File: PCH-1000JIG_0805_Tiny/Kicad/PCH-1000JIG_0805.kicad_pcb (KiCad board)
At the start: 2 copper layers, 23.1 x 11.3 mm, 14 parts

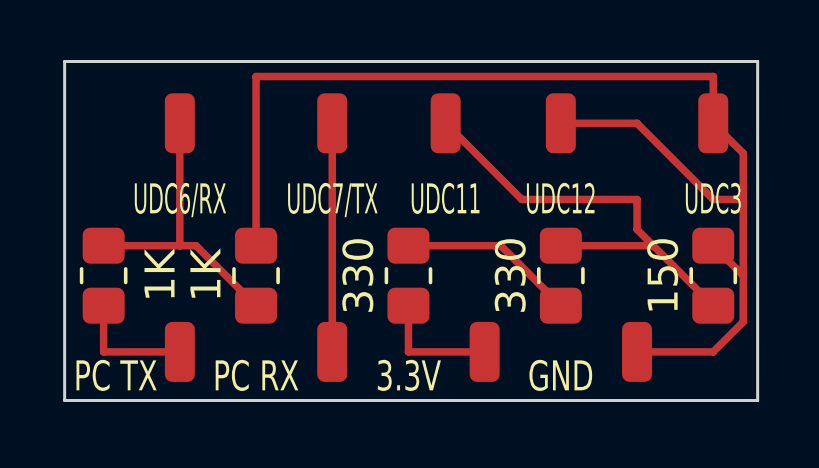
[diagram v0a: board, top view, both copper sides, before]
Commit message: Revision 2.2a of the tiny board.
Footprint reduced from 23.1 x 11.3mm(0.91 x 0.44 inches) to 19.3 x 11mm(0.76 x 0.43 inches)
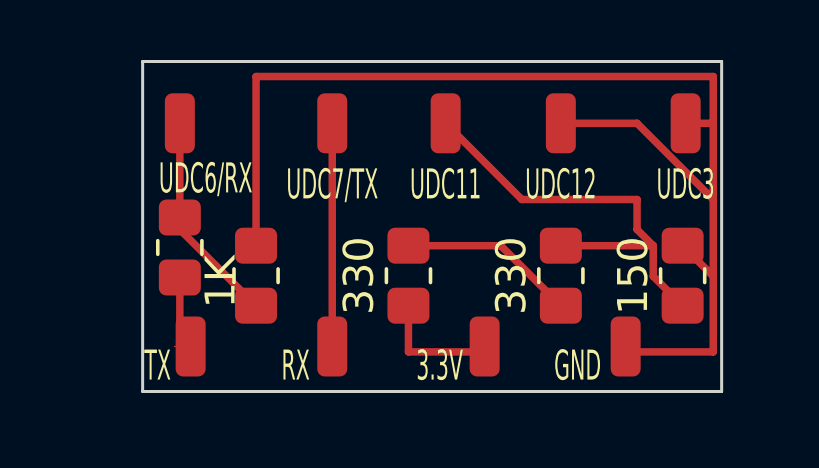
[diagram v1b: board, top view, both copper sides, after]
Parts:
- RX: renamed from PC RX
- TX: renamed from PC TX
- moved 1K 2.71 mm to (40.6, 39.7)
- moved 150 1.02 mm to (57.4, 40.6)
- moved UDC3 0.92 mm to (57.5, 35.6)
- moved GND 0.42 mm to (55.5, 43.0)
- moved TX 0.40 mm to (41.0, 43.0)
- moved 3.3V 0.18 mm to (50.8, 43.0)
- moved RX 0.18 mm to (45.7, 43.0)
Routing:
- net (no net): track 88.8 -> 84.7 mm
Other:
- board size 23.1 x 11.3 mm -> 19.3 x 11 mm
- board text added: "PCH-1000JIG Rev 2.2a by Mathieulh"
- board text removed: "PCH-1000JIG Rev 2.1a by Mathieulh"

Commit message: Changed silkscreen
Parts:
- PC RX: renamed from RX
- PC TX: renamed from TX
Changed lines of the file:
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@@
     (tags "MesurementPoint Square SMDPad 1mmx2mm ")
     (attr exclude_from_pos_files exclude_from_bom)
-    (fp_text reference "3.3V" (at -1.5 0.64) (layer "F.SilkS")
+    (fp_text reference "3.3V" (at 1.6 0.64) (layer "F.SilkS")
         (effects (font (size 1 0.5) (thickness 0.15)))
     )
@@
     (tags "MesurementPoint Square SMDPad 1mmx2mm ")
     (attr exclude_from_pos_files exclude_from_bom)
-    (fp_text reference "RX" (at -1.22 0.64) (layer "F.SilkS")
+    (fp_text reference "PC RX" (at 1.88 0.64) (layer "F.SilkS")
         (effects (font (size 1 0.5) (thickness 0.15)))
     )
@@
     (tags "MesurementPoint Square SMDPad 1mmx2mm ")
     (attr exclude_from_pos_files exclude_from_bom)
-    (fp_text reference "GND" (at -1.6 0.64) (layer "F.SilkS")
+    (fp_text reference "GND" (at 1.6 0.64) (layer "F.SilkS")
         (effects (font (size 1 0.5) (thickness 0.15)))
     )
@@
     (tags "MesurementPoint Square SMDPad 1mmx2mm ")
     (attr exclude_from_pos_files exclude_from_bom)
-    (fp_text reference "TX" (at -1.1 0.64) (layer "F.SilkS")
+    (fp_text reference "PC TX" (at 1.9 0.64) (layer "F.SilkS")
         (effects (font (size 1 0.5) (thickness 0.15)))
     )

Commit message: fixed a trace
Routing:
- net (no net): track 84.7 -> 88.7 mm
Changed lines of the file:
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@@
   (segment (start 52.04 38.1) (end 49.5 35.56) (width 0.25) (layer "F.Cu") (net 0))
   (segment (start 55.88 39.1) (end 55.88 38.1) (width 0.25) (layer "F.Cu") (net 0))
+  (segment (start 40.64 39.1) (end 42.68 41.14) (width 0.25) (layer "F.Cu") (net 0))
+  (segment (start 41.8 35.56) (end 41.8 40.26) (width 0.25) (layer "F.Cu") (net 0))
   (segment (start 48.26 39.64) (end 51.34 39.64) (width 0.25) (layer "F.Cu") (net 0))
   (segment (start 40.64 40.7) (end 40.64 42.64) (width 0.25) (layer "F.Cu") (net 0))
@@
   (segment (start 41 43) (end 40.46 43) (width 0) (layer "F.Cu") (net 0))
   (segment (start 40.64 42.64) (end 41 43) (width 0) (layer "F.Cu") (net 0))
-  (segment (start 40.64 39.1) (end 43.18 41.64) (width 0.25) (layer "F.Cu") (net 0))
-  (segment (start 40.64 35.56) (end 40.64 38.7) (width 0.25) (layer "F.Cu") (net 0))
   (segment (start 41 40.86) (end 40.64 40.5) (width 0) (layer "F.Cu") (net 0))
   (segment (start 56.42 39.64) (end 55.88 39.1) (width 0.25) (layer "F.Cu") (net 0))
   (segment (start 55.88 38.1) (end 52.04 38.1) (width 0.25) (layer "F.Cu") (net 0))
   (segment (start 48.26 41.64) (end 48.26 43.18) (width 0.25) (layer "F.Cu") (net 0))
+  (segment (start 40.64 35.56) (end 41.8 35.56) (width 0.25) (layer "F.Cu") (net 0))
   (segment (start 58.4 40.64) (end 57.4 39.64) (width 0.25) (layer "F.Cu") (net 0))
+  (segment (start 41.8 40.26) (end 42.68 41.14) (width 0.25) (layer "F.Cu") (net 0))
   (segment (start 58.42 35.56) (end 58.42 38.1) (width 0.25) (layer "F.Cu") (net 0))
   (segment (start 53.34 35.56) (end 55.88 35.56) (width 0.25) (layer "F.Cu") (net 0))
   (segment (start 50.62 43.18) (end 50.8 43) (width 0.25) (layer "F.Cu") (net 0))
+  (segment (start 42.68 41.14) (end 43.18 41.64) (width 0.25) (layer "F.Cu") (net 0))
   (segment (start 45.72 35.56) (end 45.72 43) (width 0.25) (layer "F.Cu") (net 0))
 )

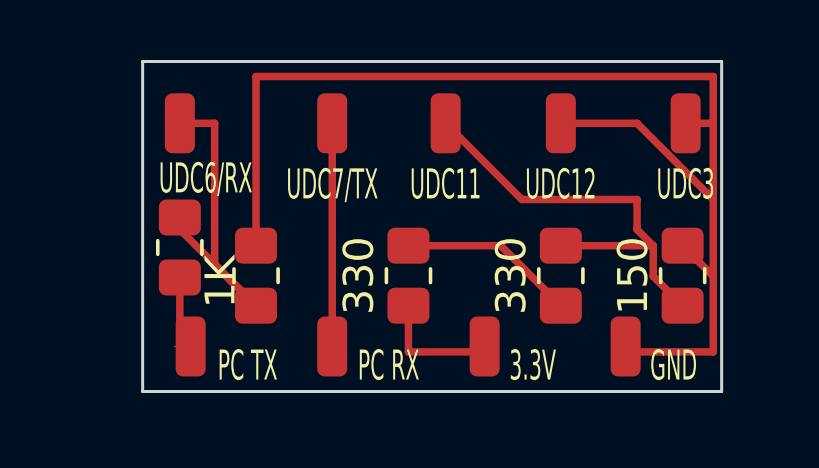
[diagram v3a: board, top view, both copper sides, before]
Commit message: Reduced footprint to 17.3 x 11mm(0.68 x 0.43 inches). (rev 2.2b)
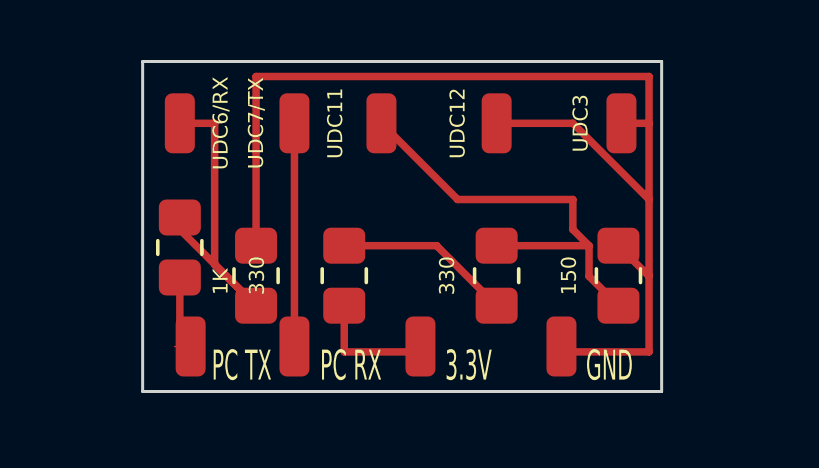
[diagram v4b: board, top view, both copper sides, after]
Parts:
- moved 150 2.14 mm to (55.3, 40.6)
- moved 3.3V 2.14 mm to (48.7, 43.0)
- moved 330 2.14 mm to (51.2, 40.6)
- moved 330 2.14 mm to (46.1, 40.6)
- moved GND 2.14 mm to (53.4, 43.0)
- moved UDC11 2.14 mm to (47.4, 35.6)
- moved UDC12 2.14 mm to (51.2, 35.6)
- moved UDC3 2.14 mm to (55.4, 35.6)
- moved PC RX 1.26 mm to (44.5, 43.0)
- moved UDC7/TX 1.26 mm to (44.5, 35.6)
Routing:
- net (no net): track 88.7 -> 86.5 mm
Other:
- board size 19.3 x 11 mm -> 17.3 x 11 mm
- board text added: "PCH-1000JIG Rev 2.2b by Mathieulh"
- board text removed: "PCH-1000JIG Rev 2.2a by Mathieulh"

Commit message: fixed silkscreen
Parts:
- 2 x 1K: renamed from 1K
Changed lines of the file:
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@@
     (tags "resistor handsolder")
     (attr smd)
-    (fp_text reference "1K" (at -1.14 1.36 90) (layer "F.SilkS")
+    (fp_text reference "2 x 1K" (at 0.227064 1.36 270) (layer "F.SilkS")
         (effects (font (size 0.5 0.5) (thickness 0.15)))
     )
@@
     (tags "resistor handsolder")
     (attr smd)
-    (fp_text reference "330" (at 0 -2.91 90) (layer "F.SilkS")
+    (fp_text reference "330" (at 0 1.58 90) (layer "F.SilkS")
         (effects (font (size 0.5 0.5) (thickness 0.15)))
     )

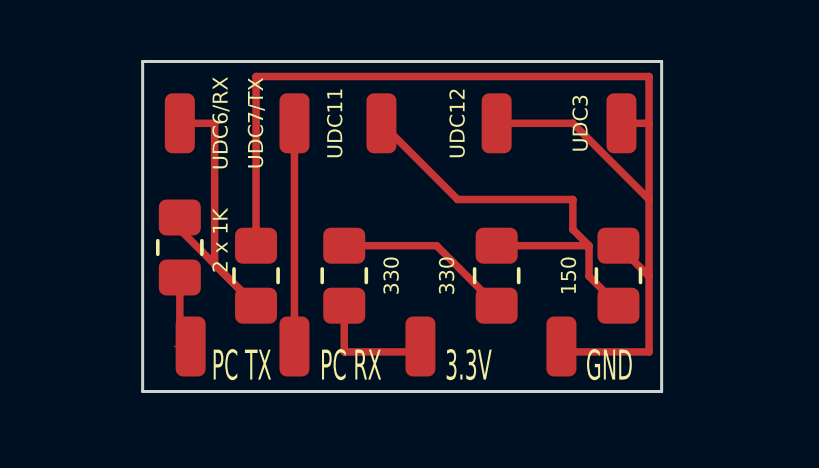
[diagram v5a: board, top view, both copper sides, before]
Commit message: footprint reduced to16.6 x 11mm(0.65 x 0.43 inches).
16.6 x 11mm(0.65 x 0.43 inches).
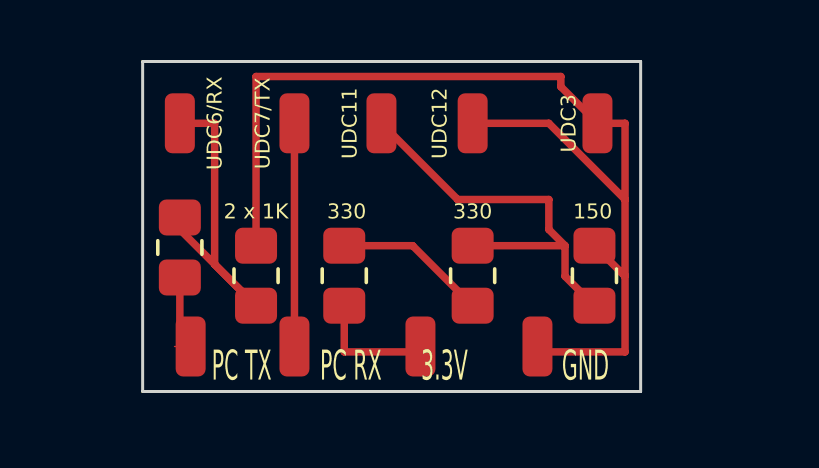
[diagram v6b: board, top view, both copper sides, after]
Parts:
- moved 330 0.80 mm to (50.4, 40.6)
- moved UDC12 0.80 mm to (50.4, 35.6)
- moved 150 0.80 mm to (54.5, 40.6)
- moved GND 0.80 mm to (52.6, 43.0)
- moved UDC3 0.80 mm to (54.6, 35.6)
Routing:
- net (no net): track 86.5 -> 82.5 mm
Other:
- board size 17.3 x 11 mm -> 16.6 x 11 mm

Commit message: Made more clearance for easier soldering.
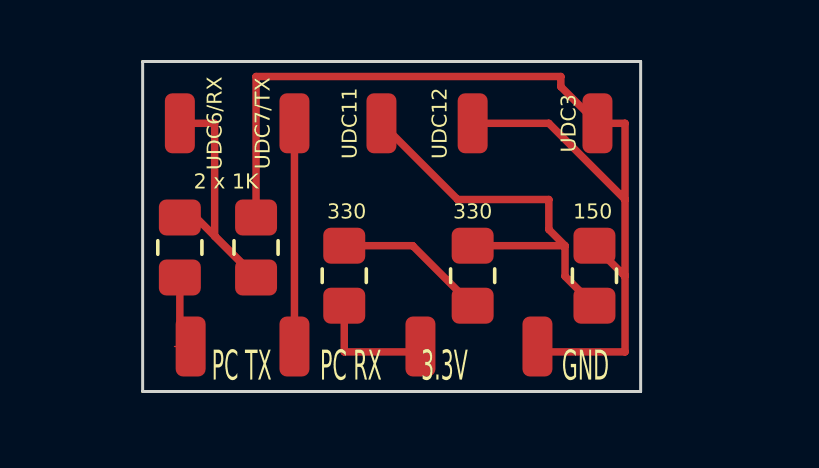
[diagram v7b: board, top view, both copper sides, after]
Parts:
- moved 1K 0.94 mm to (43.2, 39.7)
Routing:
- net (no net): track 82.5 -> 81.1 mm
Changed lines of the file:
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@@
     (tags "resistor handsolder")
     (attr smd)
-    (fp_text reference "2 x 1K" (at 1.2 2.54 180) (layer "F.SilkS")
+    (fp_text reference "2 x 1K" (at 2.2 1.54 180) (layer "F.SilkS")
         (effects (font (size 0.5 0.5) (thickness 0.15)))
     )
@@
   )
   (footprint "Resistor_SMD:R_0805_2012Metric_Pad1.20x1.40mm_HandSolder" (layer "F.Cu")
-    (at 43.18 40.64 90)
+    (at 43.18 39.7 90)
     (descr "Resistor SMD 0805 (2012 Metric), square (rectangular) end terminal, IPC_7351 nominal with elongated pad for handsoldering. (Body size source: IPC-SM-782 page 72, https://www.pcb-3d.com/wordpress/wp-content/uploads/ipc-sm-782a_amendment_1_and_2.pdf), generated with kicad-footprint-generator")
     (tags "resistor handsolder")
@@
   (segment (start 52.94 39.1) (end 52.94 38.1) (width 0.25) (layer "F.Cu") (net 0))
   (segment (start 53.34 34.34) (end 54.56 35.56) (width 0.25) (layer "F.Cu") (net 0))
-  (segment (start 40.64 39.1) (end 42.68 41.14) (width 0.25) (layer "F.Cu") (net 0))
-  (segment (start 41.8 35.56) (end 41.8 40.26) (width 0.25) (layer "F.Cu") (net 0))
   (segment (start 46.12 39.64) (end 48.4 39.64) (width 0.25) (layer "F.Cu") (net 0))
   (segment (start 40.64 40.7) (end 40.64 42.64) (width 0.25) (layer "F.Cu") (net 0))
-  (segment (start 43.18 39.64) (end 43.18 34) (width 0.25) (layer "F.Cu") (net 0))
   (segment (start 53.48 40.66) (end 54.46 41.64) (width 0.25) (layer "F.Cu") (net 0))
   (segment (start 55.48 35.56) (end 54.56 35.56) (width 0.25) (layer "F.Cu") (net 0))
@@
   (segment (start 50.4 39.64) (end 53.48 39.64) (width 0.25) (layer "F.Cu") (net 0))
   (segment (start 41 43.18) (end 40.64 43.18) (width 0) (layer "F.Cu") (net 0))
+  (segment (start 41.8 35.56) (end 41.8 39.32) (width 0.25) (layer "F.Cu") (net 0))
   (segment (start 53.48 39.64) (end 53.48 40.66) (width 0.25) (layer "F.Cu") (net 0))
   (segment (start 55.48 40.64) (end 55.48 43.18) (width 0.25) (layer "F.Cu") (net 0))
@@
   (segment (start 40.64 42.64) (end 41 43) (width 0) (layer "F.Cu") (net 0))
   (segment (start 41 40.86) (end 40.64 40.5) (width 0) (layer "F.Cu") (net 0))
+  (segment (start 40.64 38.7) (end 41.18 38.7) (width 0.25) (layer "F.Cu") (net 0))
   (segment (start 53.48 39.64) (end 52.94 39.1) (width 0.25) (layer "F.Cu") (net 0))
   (segment (start 48.4 39.64) (end 50.4 41.64) (width 0.25) (layer "F.Cu") (net 0))
+  (segment (start 41.8 39.32) (end 43.15 40.67) (width 0.25) (layer "F.Cu") (net 0))
   (segment (start 46.12 41.64) (end 46.12 43.18) (width 0.25) (layer "F.Cu") (net 0))
   (segment (start 40.64 35.56) (end 41.8 35.56) (width 0.25) (layer "F.Cu") (net 0))
   (segment (start 55.46 40.64) (end 54.46 39.64) (width 0.25) (layer "F.Cu") (net 0))
   (segment (start 52.94 38.1) (end 49.9 38.1) (width 0.25) (layer "F.Cu") (net 0))
-  (segment (start 41.8 40.26) (end 42.68 41.14) (width 0.25) (layer "F.Cu") (net 0))
   (segment (start 55.48 35.56) (end 55.48 38.1) (width 0.25) (layer "F.Cu") (net 0))
   (segment (start 50.4 35.56) (end 52.94 35.56) (width 0.25) (layer "F.Cu") (net 0))
   (segment (start 53.34 34) (end 53.34 34.34) (width 0.25) (layer "F.Cu") (net 0))
   (segment (start 48.48 43.18) (end 48.66 43) (width 0.25) (layer "F.Cu") (net 0))
-  (segment (start 42.68 41.14) (end 43.18 41.64) (width 0.25) (layer "F.Cu") (net 0))
+  (segment (start 43.15 40.67) (end 43.18 40.7) (width 0.25) (layer "F.Cu") (net 0))
   (segment (start 43.18 34) (end 53.34 34) (width 0.25) (layer "F.Cu") (net 0))
+  (segment (start 43.18 34) (end 43.18 38.7) (width 0.25) (layer "F.Cu") (net 0))
+  (segment (start 41.18 38.7) (end 43.15 40.67) (width 0.25) (layer "F.Cu") (net 0))
   (segment (start 44.46 35.56) (end 44.46 43) (width 0.25) (layer "F.Cu") (net 0))
 )

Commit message: updated silkscreen
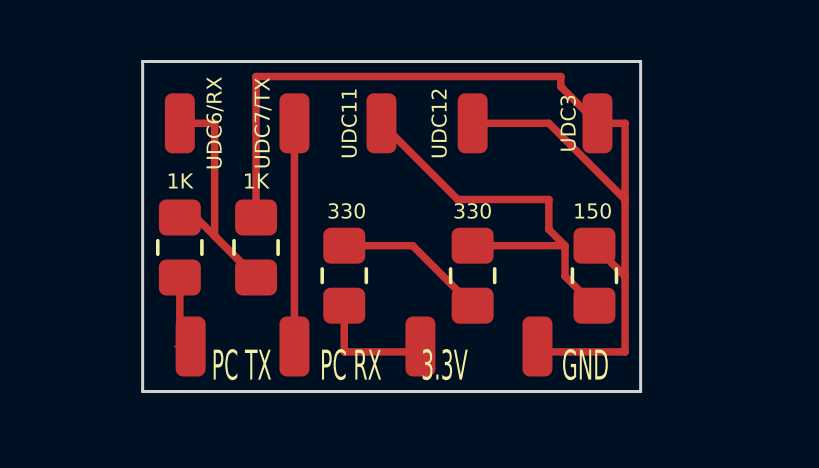
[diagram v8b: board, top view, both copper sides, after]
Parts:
- 1K: renamed from 2 x 1K
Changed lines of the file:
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@@
     (tags "resistor handsolder")
     (attr smd)
-    (fp_text reference "2 x 1K" (at 2.2 1.54 180) (layer "F.SilkS")
+    (fp_text reference "1K" (at 2.2 2.54 180) (layer "F.SilkS")
         (effects (font (size 0.5 0.5) (thickness 0.15)))
     )
@@
     (tags "resistor handsolder")
     (attr smd)
-    (fp_text reference "1K" (at 0 -1.65 90) (layer "Cmts.User")
-        (effects (font (size 1 1) (thickness 0.15)))
+    (fp_text reference "1K" (at 2.2 -2.54) (layer "F.SilkS")
+        (effects (font (size 0.5 0.5) (thickness 0.15)))
     )
     (fp_text value "R_0805_2012Metric_Pad1.20x1.40mm_HandSolder" (at -2.54 0.39 90) (layer "F.Fab")
